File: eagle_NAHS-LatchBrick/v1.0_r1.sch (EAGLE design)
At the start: 34 parts, among them IC1 ESP12F, IC2 TP4056, IC3 DW01A, IC4 FT232RL, IC5 ATTINY212-SSNR, J1 10118194-0001LF, Q1 8205A

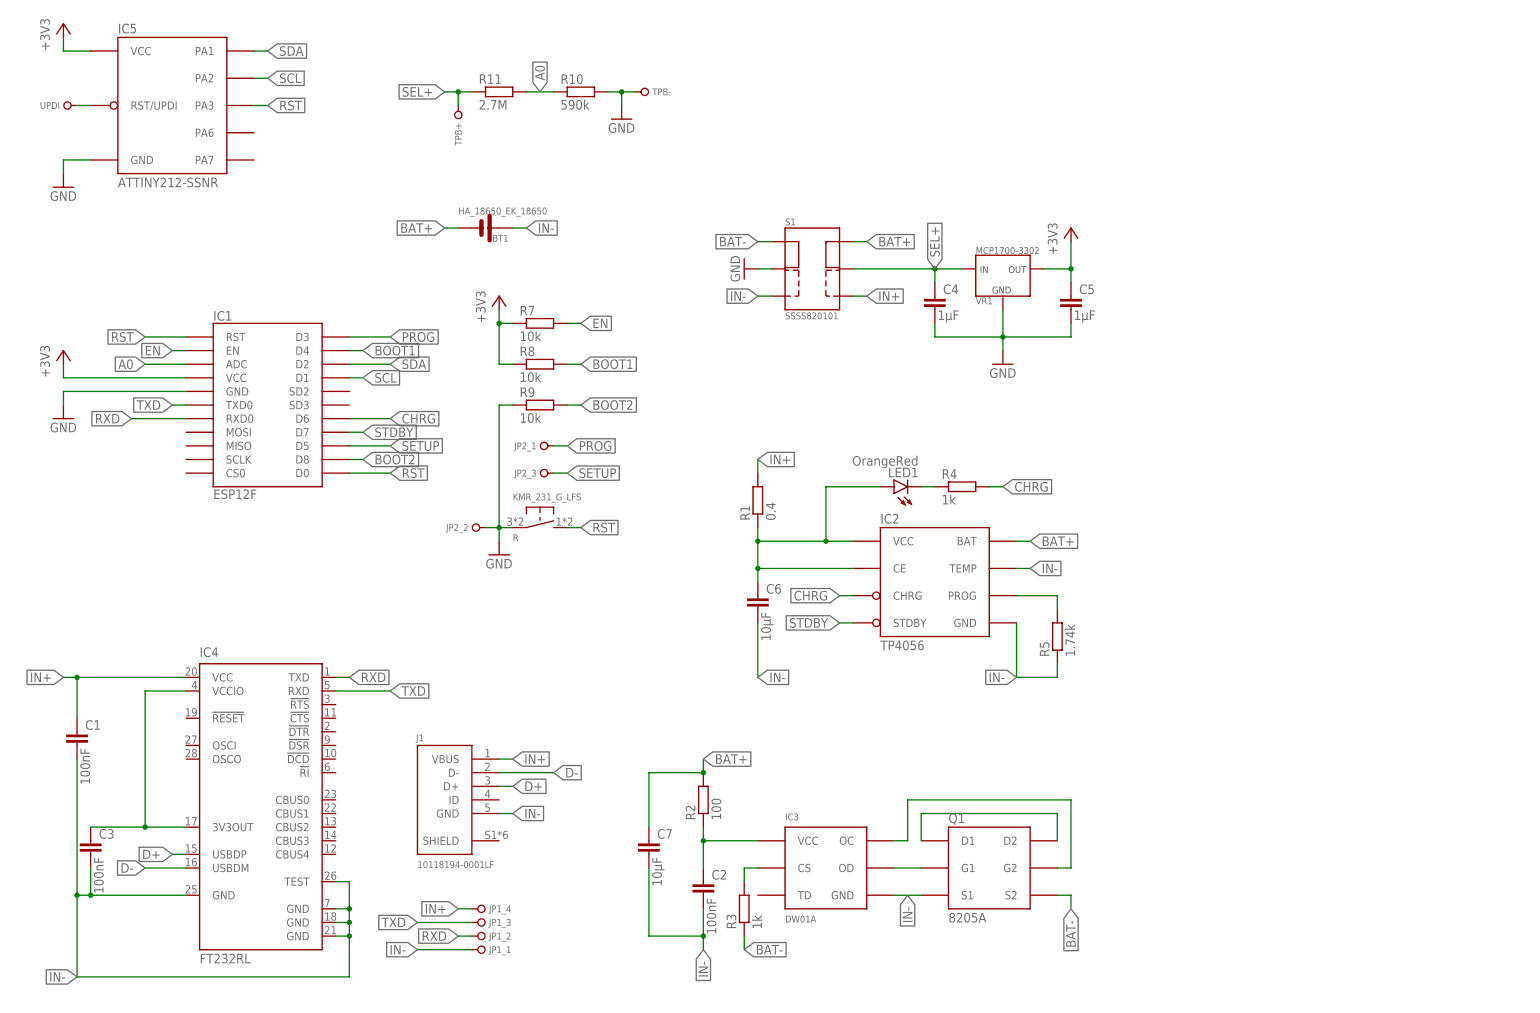
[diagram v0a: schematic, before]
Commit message: Board v1.0_R1 should allready be finished
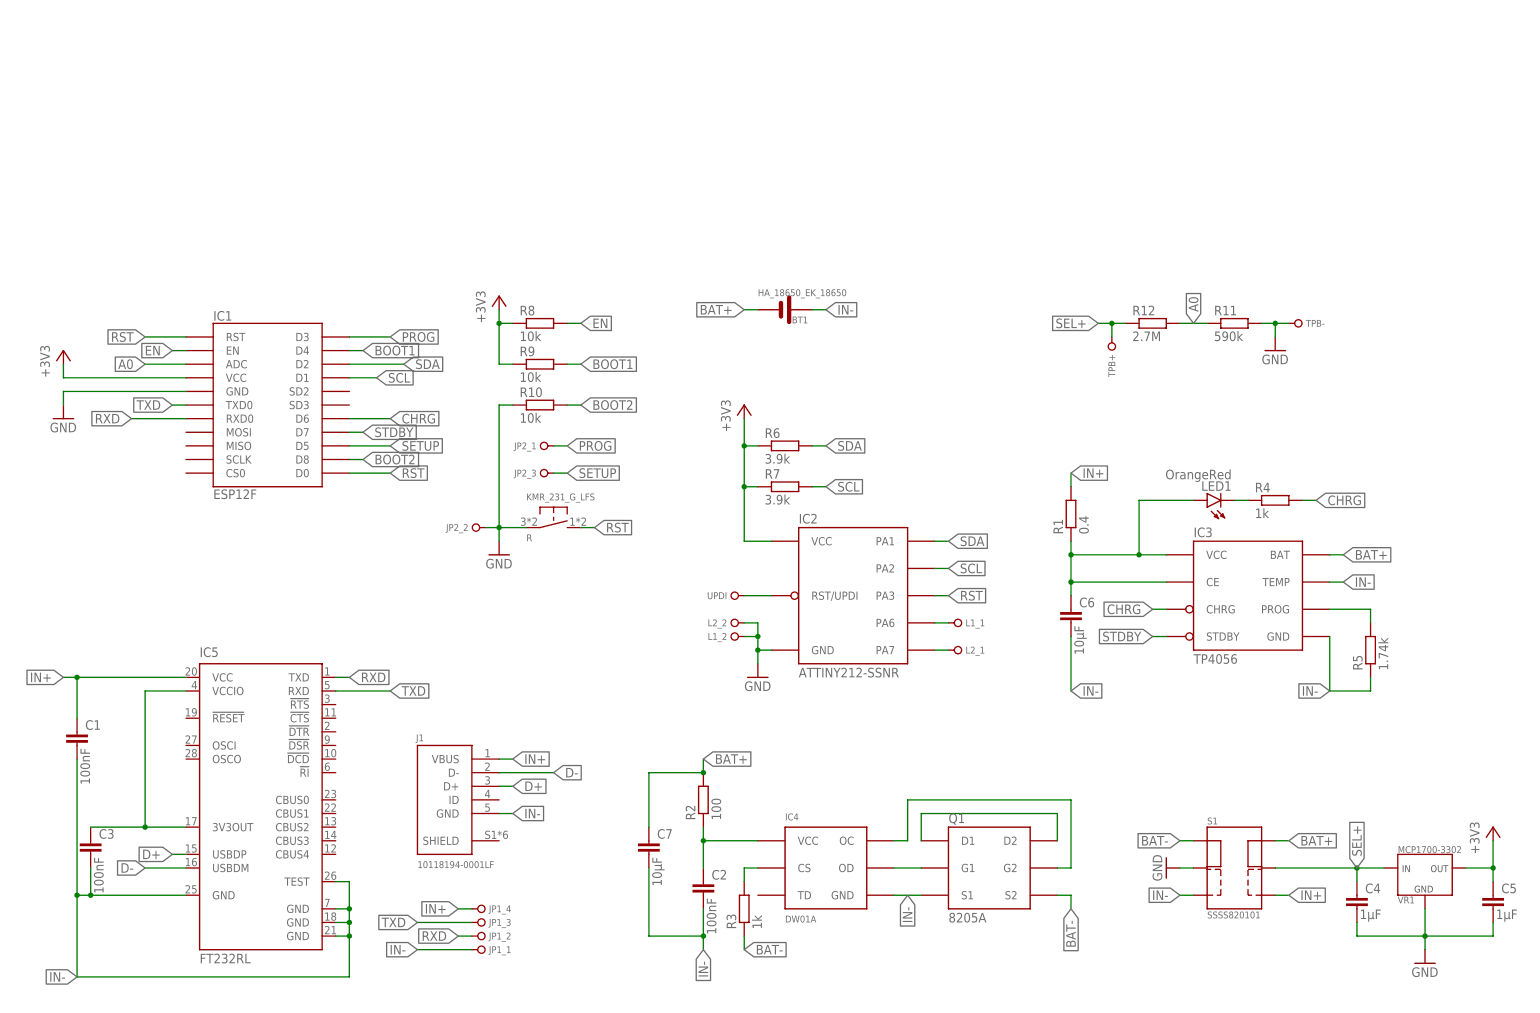
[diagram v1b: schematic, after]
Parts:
- added L1, L2: PINHD_1X02_R_1, no_pinhd:PINHD_1X02_R_1
- added R12: 2.7M, rcl:R-EU_R0805
- added R6: 3.9k, rcl:R-EU_R0805
- IC2: value TP4056 -> ATTINY212-SSNR; device no_reichelt:TP4056 -> no_microchip:ATTINY212-SSNR
- IC3: value DW01A -> TP4056; device no_reichelt:DW01A -> no_reichelt:TP4056
- IC4: value FT232RL -> DW01A; device ftdichip:FT232RL -> no_reichelt:DW01A
- IC5: value ATTINY212-SSNR -> FT232RL; device no_microchip:ATTINY212-SSNR -> ftdichip:FT232RL
- R10: value 590k -> 10k
- R11: value 2.7M -> 590k
- R7: value 10k -> 3.9k
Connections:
- removed net N$5: IC5.RST/UPDI, UPDI.1
- removed net N$6: C3.1, IC4.3V3OUT, IC4.VCCIO
- new net L1: IC2.PA6, L1_1.1
- new net L2: IC2.PA7, L2_1.1
- new net UPDI: IC2.RST/UPDI, UPDI.1
- new net VCCIO: C3.1, IC5.3V3OUT, IC5.VCCIO
- net +3V3: now also IC2.VCC, R6.1, R9.1; no longer IC5.VCC
- net A0: now also R11.1, R12.2; no longer R10.1, R11.2
- net BAT+: now also IC3.BAT; no longer IC2.BAT
- net BOOT1: now also R9.2; no longer R8.2
- net BOOT2: now also R10.2; no longer R9.2
- net CHRG: now also IC3.CHRG; no longer IC2.CHRG
- net D+: now also IC5.USBDP; no longer IC4.USBDP
- net D-: now also IC5.USBDM; no longer IC4.USBDM
- net EN: now also R8.2; no longer R7.2
- net GND: now also IC2.GND, L1_2.1, L2_2.1, R10.1, R11.2; no longer IC5.GND, R10.2, R9.1
- net IN+: now also IC5.VCC; no longer IC4.VCC
- net IN-: now also IC3.TEMP, IC5.GND, IC5.GND@1, IC5.GND@2, IC5.GND@A, IC5.TEST; no longer IC2.GND, IC2.TEMP, IC4.GND@1, IC4.GND@2, IC4.GND@A, IC4.TEST
- net N$1: now also IC3.CE, IC3.VCC; no longer IC2.CE, IC2.VCC
- net N$11: now also IC4.OC; no longer IC3.OC
- net N$2: now also IC3.PROG; no longer IC2.PROG
- net N$3: now also IC4.CS; no longer IC3.CS
- net N$4: now also IC4.VCC; no longer IC3.VCC
- net N$8: now also IC4.OD; no longer IC3.OD
- net RST: now also IC2.PA3; no longer IC5.PA3
- net RXD: now also IC5.TXD; no longer IC4.TXD
- net SCL: now also IC2.PA2, R7.2; no longer IC5.PA2
- net SDA: now also IC2.PA1, R6.2; no longer IC5.PA1
- net SEL+: now also R12.1; no longer R11.1
- net STDBY: now also IC3.STDBY; no longer IC2.STDBY
- net TXD: now also IC5.RXD; no longer IC4.RXD
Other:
- moved on the sheet: BT1, C4, C5, C6, LED1, R, R1, R10, R11, R4, R5, R7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
